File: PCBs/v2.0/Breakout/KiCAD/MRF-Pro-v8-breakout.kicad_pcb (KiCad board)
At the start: 2 copper layers, 21 x 15.5 mm, 12 parts, among them J5 FPC 8P Connector, J6 Stemma QT, J7 TFS20L / DTS6012M, U1 TLV75533

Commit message: Reorient J5 on the breakout and re-plot gerbers
J5 (the FPC connector) rotated to 180 deg and repositioned. DRC clean
(0 unconnected, 0 parity). Regenerated the standalone Gerber/ set so
copper, silk and drills match the new placement.
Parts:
- moved J5 1.87 mm to (122.7, 127.3), turned to 180 degrees
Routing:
- net Net-(J5-Pin_7): track 23.6 -> 11.8 mm
- net /VBAT: track 12.5 -> 17.4 mm
- net /3.3V: track 15.9 -> 11.2 mm
- net Net-(J5-Pin_8): track 23.1 -> 18.9 mm, vias 2 -> 0
- net Net-(J5-Pin_2): track 19.3 -> 15.9 mm
- net /GND: track 26.2 -> 29.4 mm
- net Net-(J5-Pin_3): track 19.7 -> 19.1 mm

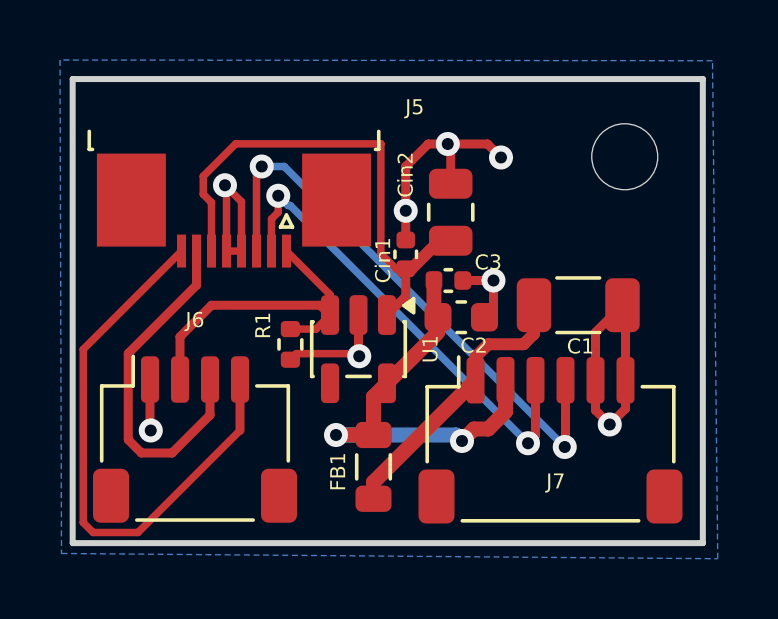
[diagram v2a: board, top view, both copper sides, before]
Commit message: Swap FPC pins 1 and 6, reroute both boards, re-plot fab
VBAT now lands on FPC pin 1 (beside the UART pair) and the switched 3.3 V
on pin 6 (beside the I2C pair), so the always-on battery rail no longer
runs next to the I2C lines. Both boards' schematics were tidied up and
fully rerouted; DRC passes clean on each. Gerbers and the JLCPCB position
files are re-plotted to match. The BOM is unchanged - this is a net and
placement change, not a parts change.
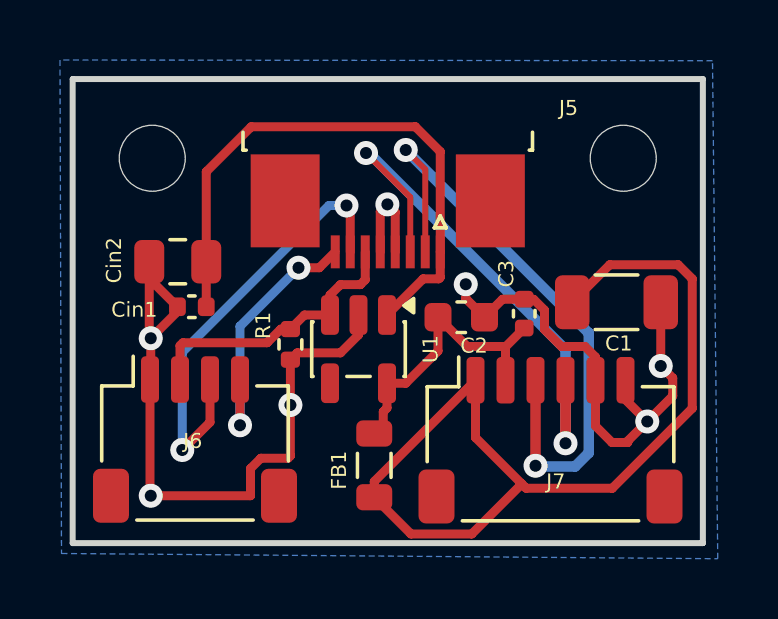
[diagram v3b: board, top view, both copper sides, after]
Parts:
- removed REF**: MountingHole_2.2mm_M2, MountingHole:MountingHole_2.2mm_M2
- added H1: MountingHole, MountingHole:MountingHole_2.2mm_M2, F.Cu at (120.0, 125.5)
- added H2: MountingHole, MountingHole:MountingHole_2.2mm_M2, F.Cu at (135.7, 125.5)
- moved Cin2 9.25 mm to (120.8, 129.0), turned to 180 degrees
- moved Cin1 7.34 mm to (121.3, 130.5), turned to 180 degrees
- moved J5 5.13 mm to (127.8, 127.3)
- moved C3 2.76 mm to (132.4, 130.7), turned to 90 degrees
- moved C1 1.28 mm to (135.4, 130.3)
- moved FB1 0.06 mm to (127.4, 135.8)
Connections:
- J5 pad 1: /3.3V -> /VBAT
- J5 pad 6: /VBAT -> /3.3V
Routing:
- net /3V3_LASER: track 9.85 -> 31.4 mm
- net /GND: track 29.4 -> 44.0 mm, vias 8 -> 7
- net Net-(J5-Pin_8): track 18.9 -> 9.03 mm, vias 0 -> 2
- net Net-(J5-Pin_2): track 15.9 -> 21.2 mm
- net /3V3_LIDAR: track 14.5 -> 9.78 mm, vias 2 -> 0
- net Net-(J5-Pin_7): track 11.8 -> 15.1 mm, vias 0 -> 2
- net /VBAT: track 17.4 -> 19.8 mm
- net /3.3V: track 11.2 -> 9.53 mm
- net Net-(J5-Pin_3): track 19.1 -> 18.5 mm
